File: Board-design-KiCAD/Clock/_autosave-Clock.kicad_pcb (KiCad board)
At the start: 2 copper layers, 13 parts, among them M1 SevSeg4Inch, M2 SevSeg4Inch, Y1 SevSeg1.8Inch, Y2 SevSeg1.8Inch, Y3 SevSeg1.8Inch, Y4 SevSeg1.8Inch

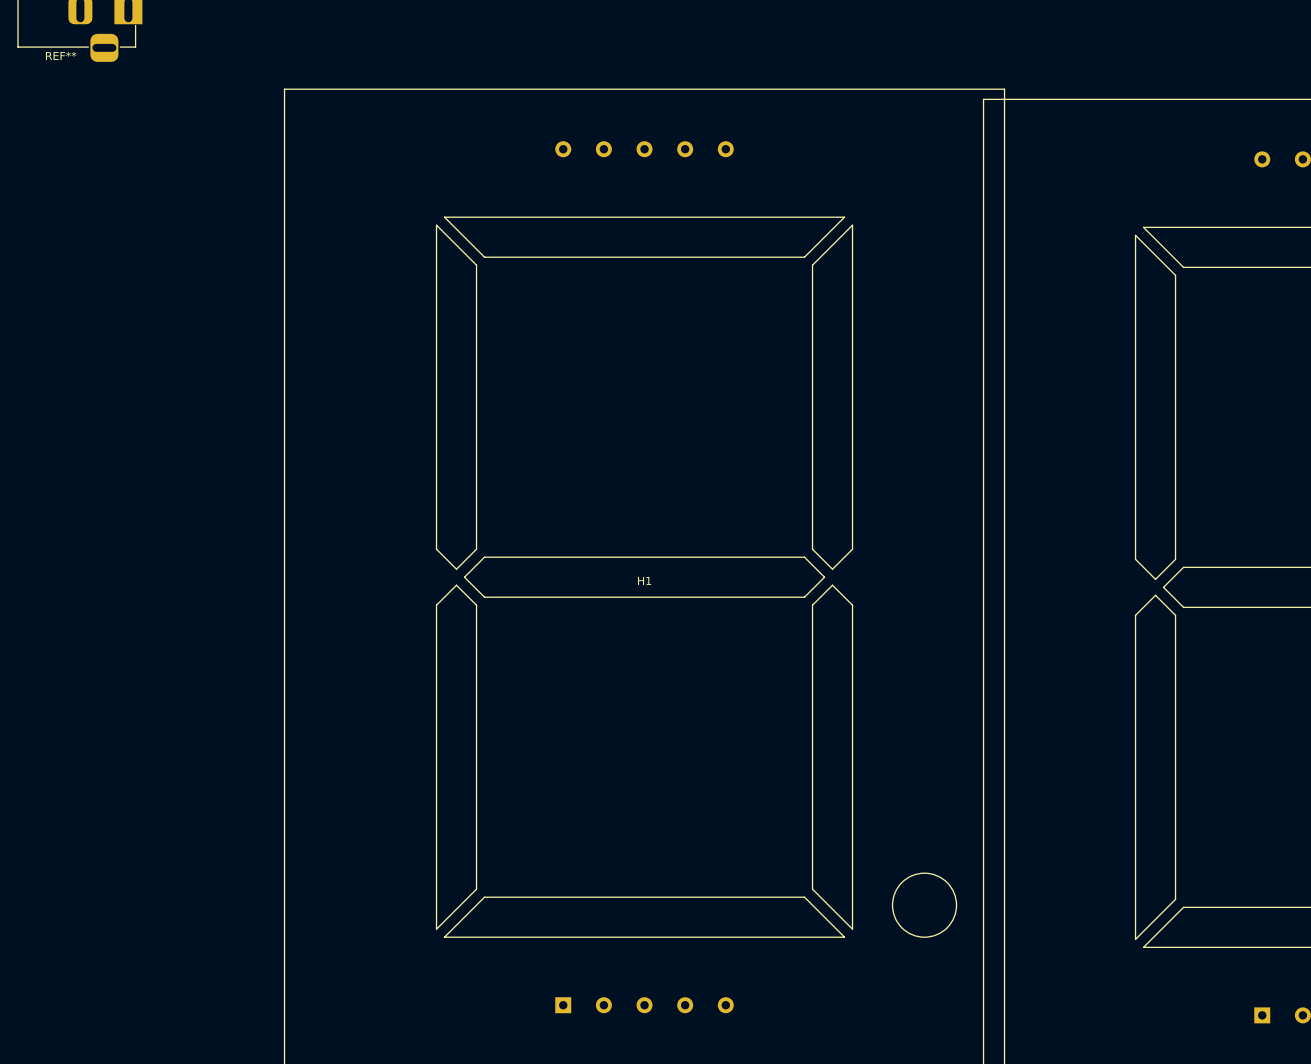
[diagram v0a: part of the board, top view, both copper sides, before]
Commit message: Add power supply and 11-V regulator
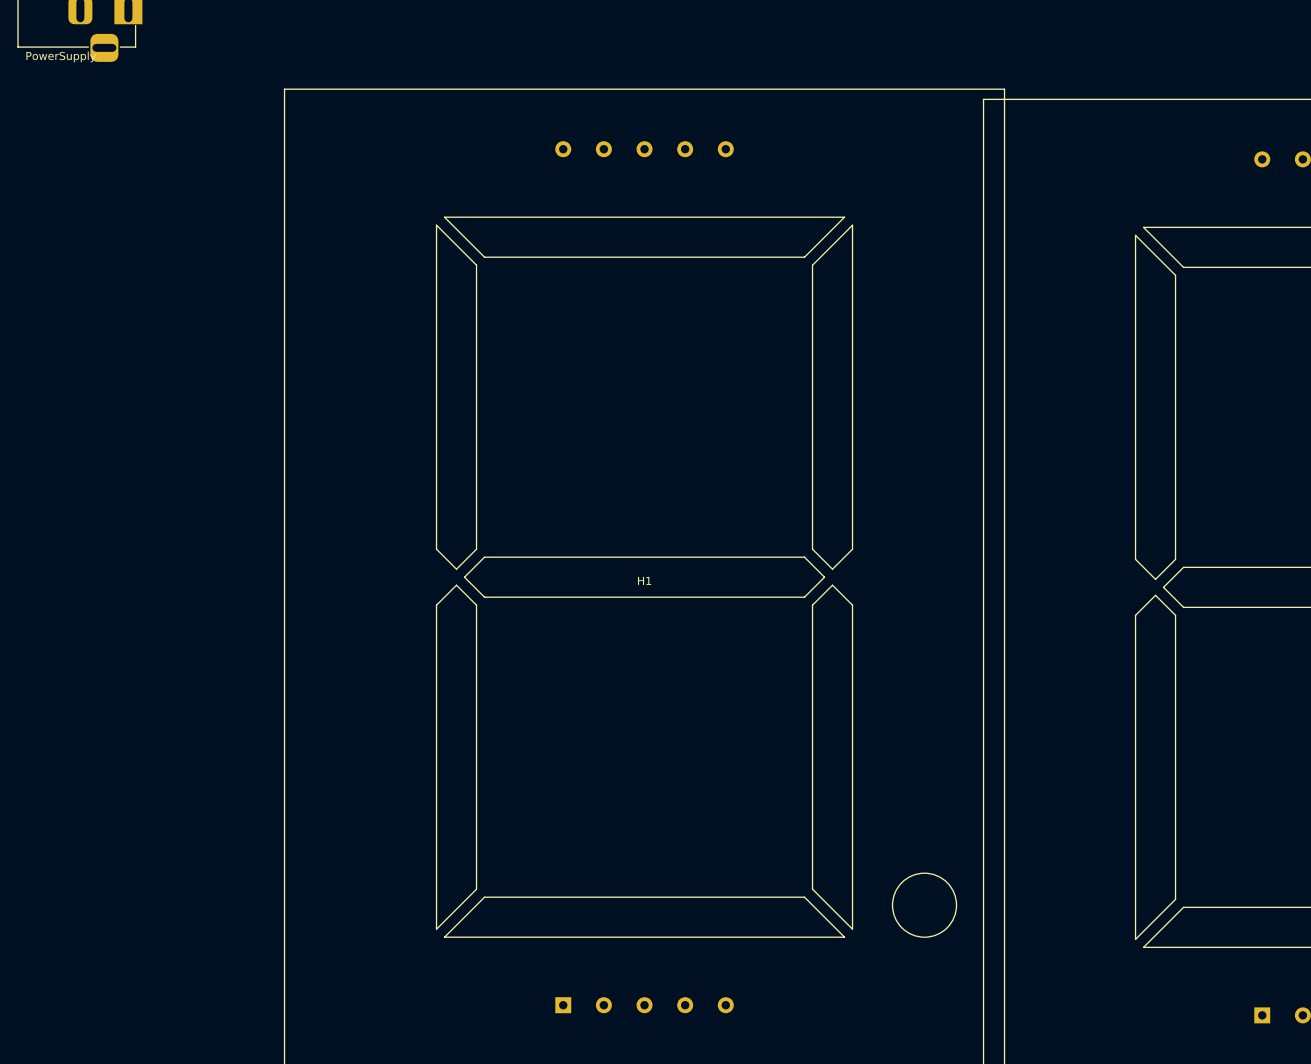
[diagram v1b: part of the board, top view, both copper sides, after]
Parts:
- renumbered REF** to PowerSupply
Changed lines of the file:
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@@
     (thickness 1.6)
     (drawings 0)
-    (tracks 0)
+    (tracks 1)
     (zones 0)
     (modules 13)
@@
     (descr "DC Barrel Jack")
     (tags "Power Jack")
-    (fp_text reference REF** (at -8.45 5.75) (layer F.SilkS)
+    (fp_text reference PowerSupply (at -8.45 5.75) (layer F.SilkS)
       (effects (font (size 1 1) (thickness 0.15)))
     )
@@
     (pad 1 thru_hole rect (at -10.16 12) (size 1.5 1.5) (drill 0.8) (layers *.Cu *.Mask))
   )
+  (segment (start 87.376 155.1) (end 87.376 154.94) (width 0.25) (layer F.Cu) (net 1))
 )
